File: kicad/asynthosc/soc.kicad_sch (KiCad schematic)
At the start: 46 parts, among them J3 Conn_ARM_SWD_TagConnect_TC203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, J4 Conn_02x07_Odd_Even, J5 Conn_02x04_Odd_Even, SW1 SW_Push, U6 STM32F723VETx, U7 W25Q32JVSS, Y1 8MHz, 8pF

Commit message: sch: pcb: tiny fixes and changes
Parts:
- added C58: 2.2u X7R, Capacitor_SMD:C_0402_1005Metric, symbol Device:C
- added J15: Conn_02x04_Odd_Even, Connector_PinHeader_2.54mm:PinHeader_2x04_P2.54mm_Vertical_SMD, symbol Connector_Generic:Conn_02x04_Odd_Even
- added R83: 3k, Resistor_SMD:R_0402_1005Metric, symbol Device:R
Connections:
- net DBG_LED: now also U6.17 (PC2)
- net GND: now also C58.2, R83.2
- net OTGHS_EXTR: now reaches U6.53 (REXTPHYHS)
- net OTGHS_EXTR: now also R83.1
- net OTGHS_VDD12: now reaches U6.55 (V12PHYHS)
- net OTGHS_VDD12: now also C58.1
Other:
- note added: "External LED GPIO"
- note added: "OTG_HS_REXT"
- note added: "VDD12OTGHS"

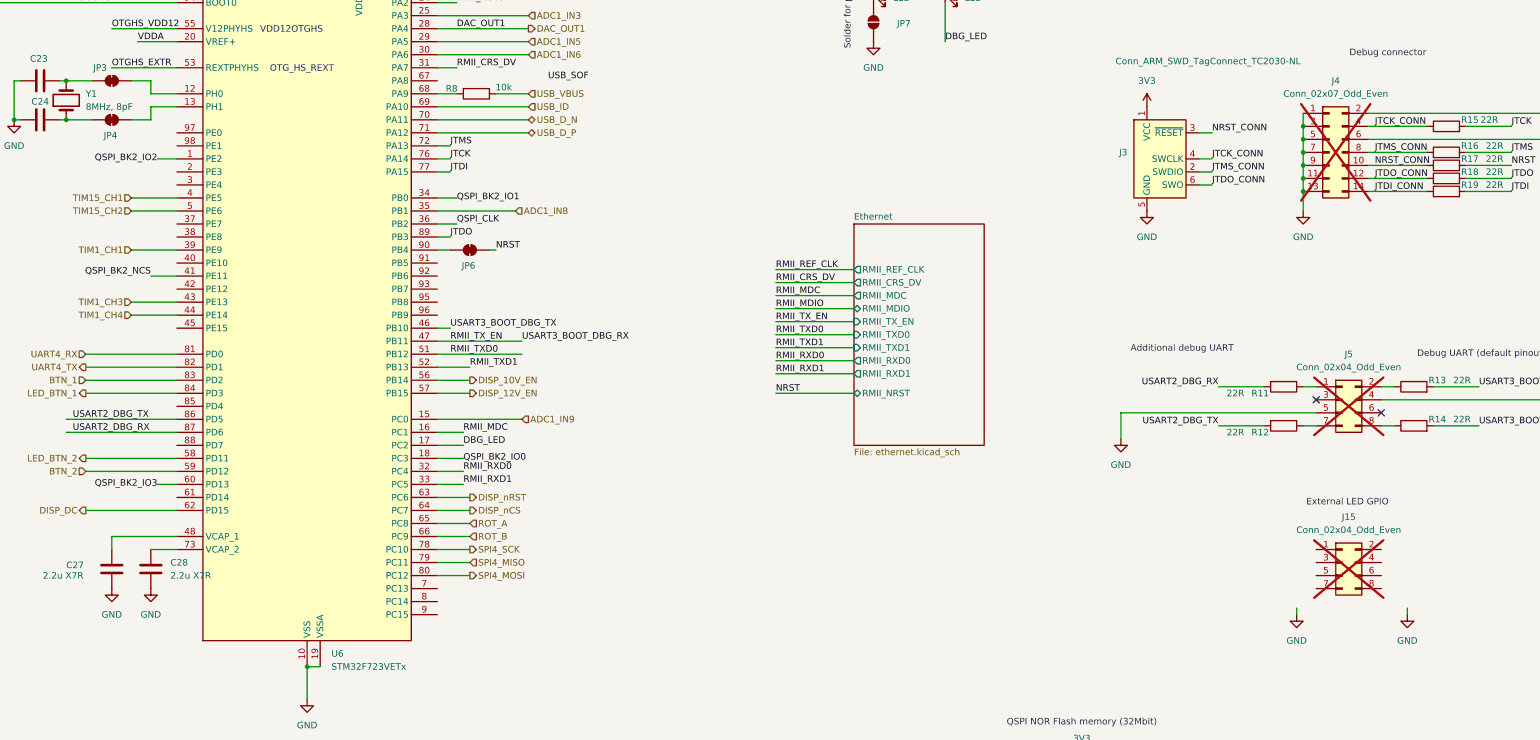
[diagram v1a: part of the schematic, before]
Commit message: sch: pcb: add gpio output connector for optional LEDs on decorative board
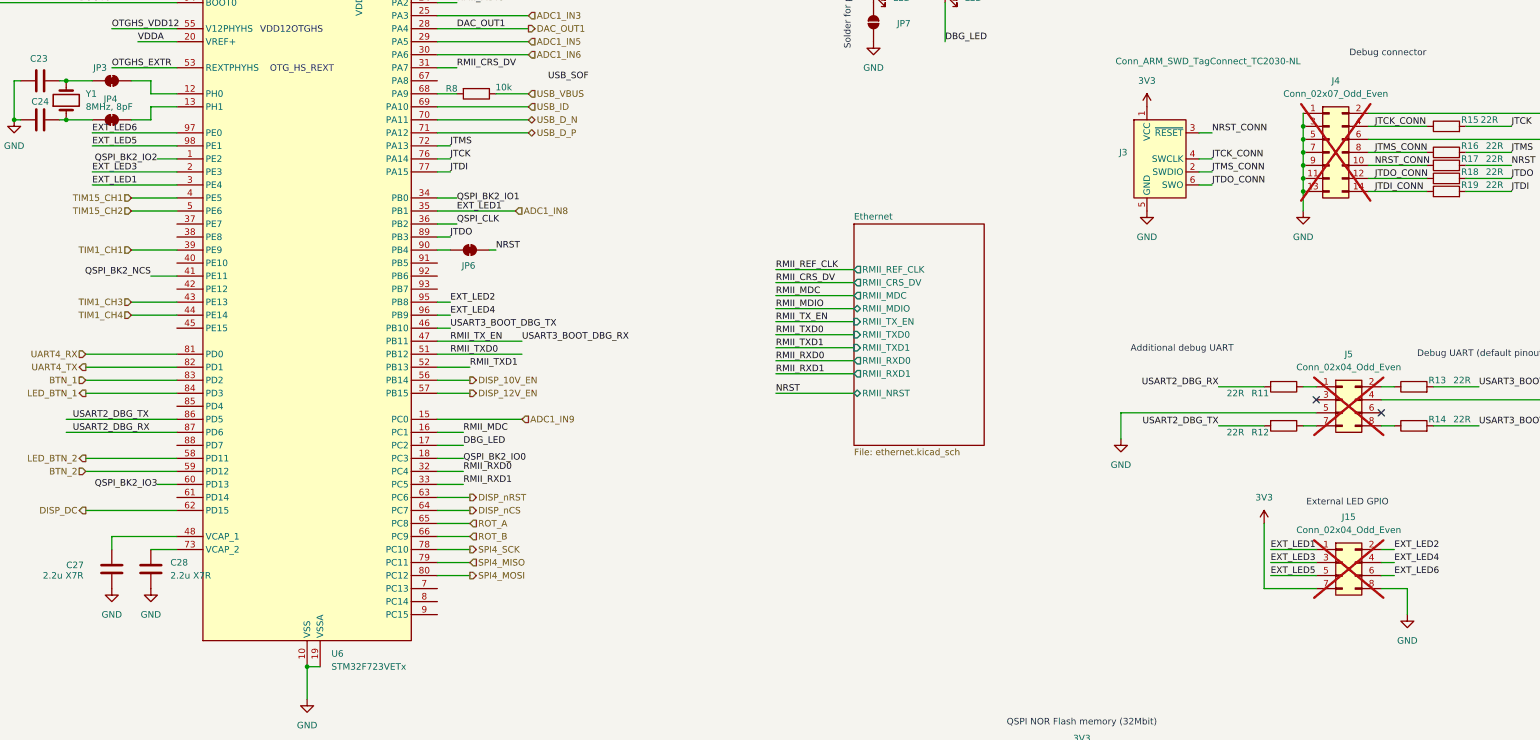
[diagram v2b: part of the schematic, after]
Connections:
- net 3V3: now also J15.7 (Pin_7)
- net ADC1_IN8: now also J15.1 (Pin_1), U6.3 (PE4)
- net GND: now also J15.8 (Pin_8)
- net EXT_LED2: now reaches J15.2 (Pin_2)
- net EXT_LED2: now also U6.95 (PB8)
- net EXT_LED3: now reaches J15.3 (Pin_3)
- net EXT_LED3: now also U6.2 (PE3)
- net EXT_LED4: now reaches J15.4 (Pin_4)
- net EXT_LED4: now also U6.96 (PB9)
- net EXT_LED5: now reaches J15.5 (Pin_5)
- net EXT_LED5: now also U6.98 (PE1)
- net EXT_LED6: now reaches J15.6 (Pin_6)
- net EXT_LED6: now also U6.97 (PE0)

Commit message: sch: pcb: wip and silkscreen cleaning
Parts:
- added JP11: SolderJumper_2_Bridged, asynthosc:SolderJumper_0402_1005Metric_Bridged, symbol Jumper:SolderJumper_2_Bridged
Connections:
- net 3V3: now also JP11.2 (B)
- net at U6.54 (VDDPHYHS): now also JP11.1 (A)
- net ADC1_IN8 renamed EXT_LED1
- net NRST renamed nRST
- net TIM15_CH1: no longer names the net of U6.4 (PE5)
- net TIM15_CH2: no longer names the net of U6.5 (PE6)
- net TIM1_CH1: no longer names the net of U6.39 (PE9)
- no-connect marks 2 -> 20

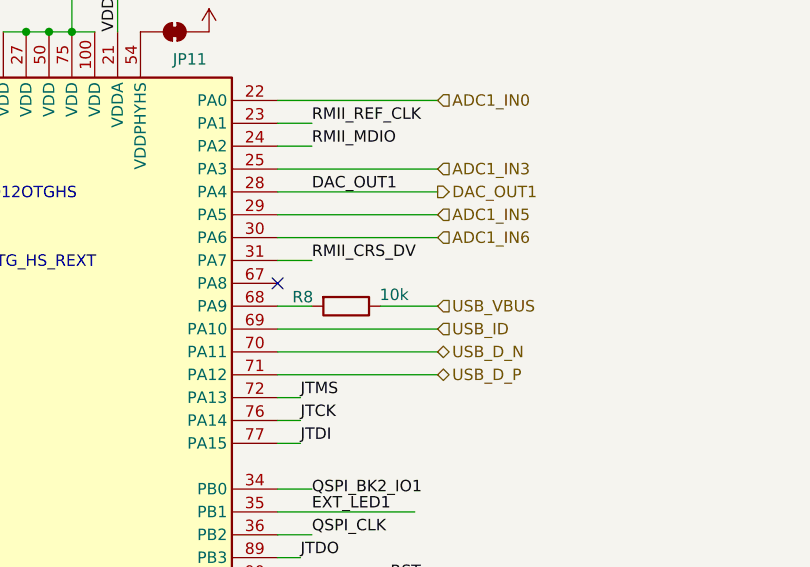
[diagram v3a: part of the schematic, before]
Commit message: sch: pcb: fix: footprint mismatches
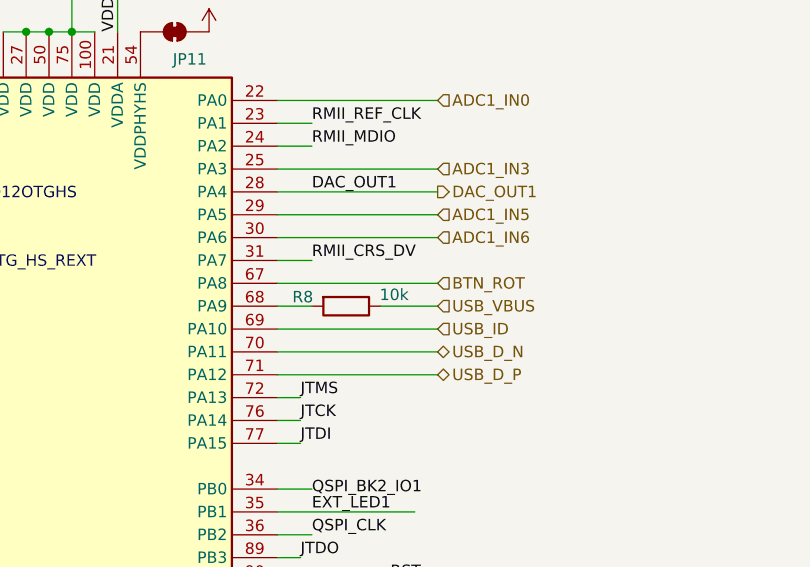
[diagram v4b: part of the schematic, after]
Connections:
- net BTN_ROT: now reaches U6.67 (PA8)
- no-connect marks 20 -> 19
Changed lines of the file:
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@@
-	)
-	(no_connect
-		(at 152.4 72.39)
 	)
 	(no_connect
@@
 		(pts
 			(xy 62.23 20.32) (xy 68.58 20.32)
+		)
+		(stroke
+			(width 0)
+			(type default)
+		)
+	)
+	(wire
+		(pts
+			(xy 152.4 72.39) (xy 170.18 72.39)
 		)
 		(stroke
@@
 		(fields_autoplaced yes)
 		(effects
+			(font
+				(size 1.27 1.27)
+			)
+			(justify left)
+		)
+	)
+	(hierarchical_label "BTN_ROT"
+		(shape input)
+		(at 170.18 72.39 0)
+		(fields_autoplaced yes)
+		(effects

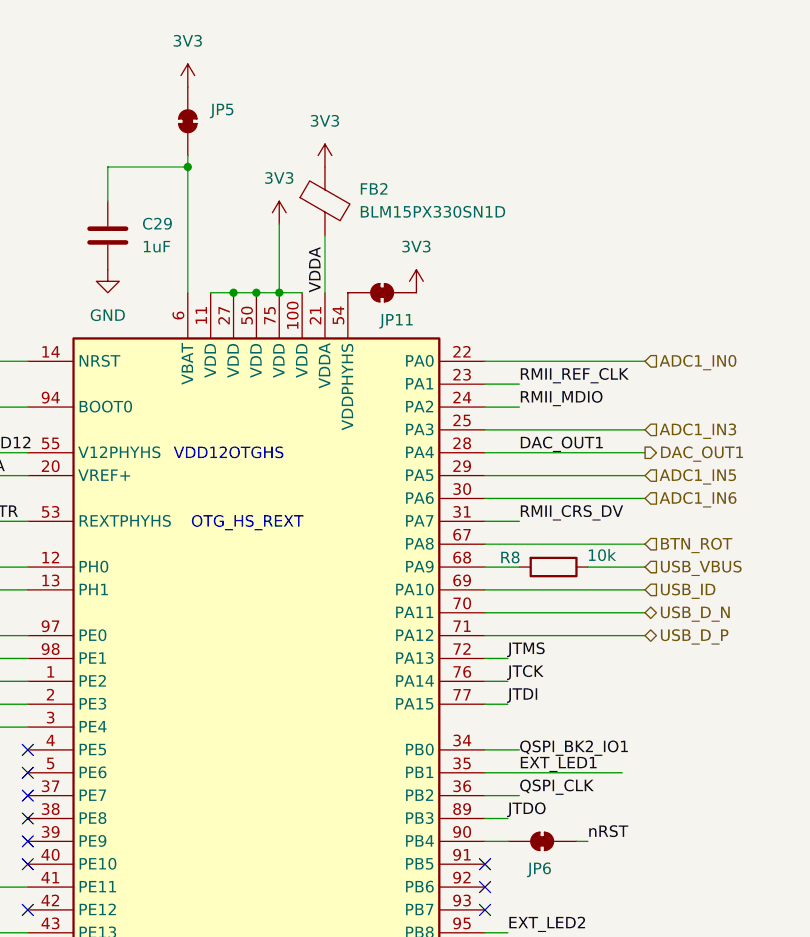
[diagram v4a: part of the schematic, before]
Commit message: pcb: route, add some silkscreen
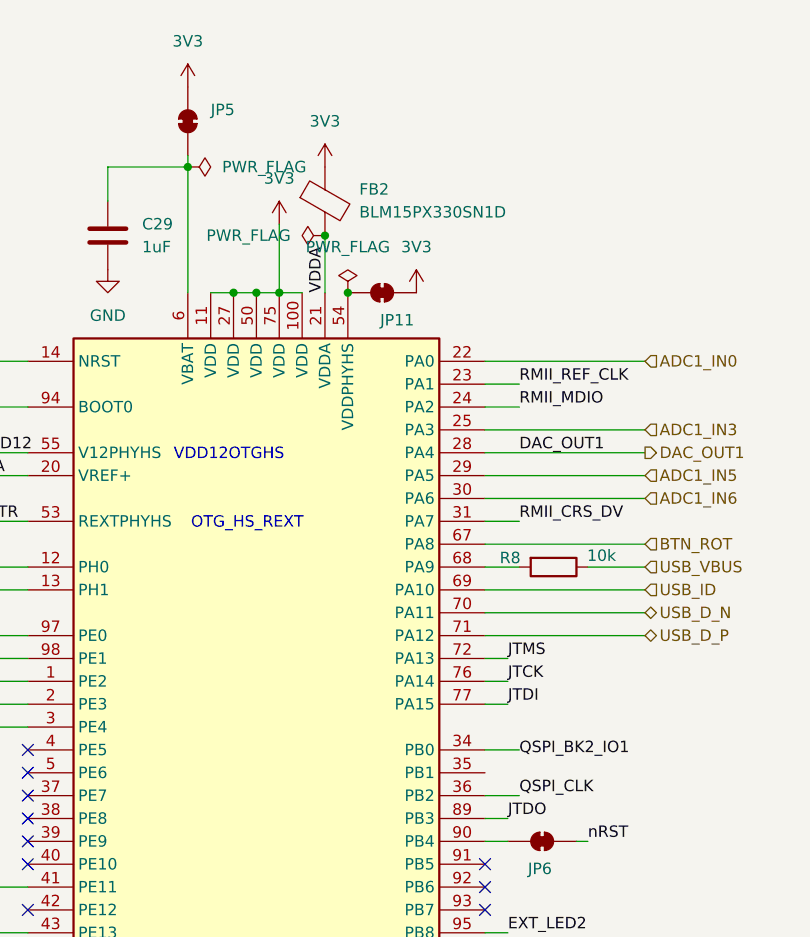
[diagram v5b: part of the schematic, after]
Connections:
- net EXT_LED1: no longer U6.35 (PB1)
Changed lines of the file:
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@@
 	)
 	(junction
+		(at 137.16 44.45)
+		(diameter 0)
+		(color 0 0 0 0)
+	)
+	(junction
 		(at 321.31 81.28)
 		(diameter 0)
@@
 	)
 	(junction
+		(at 134.62 38.1)
+		(diameter 0)
+		(color 0 0 0 0)
+	)
+	(junction
 		(at 321.31 91.44)
 		(diameter 0)
@@
 	(wire
 		(pts
-			(xy 152.4 97.79) (xy 167.64 97.79)
-		)
-		(stroke
-			(width 0)
-			(type default)
-		)
-	)
-	(wire
-		(pts
 			(xy 152.4 87.63) (xy 154.94 87.63)
 		)
@@
 		)
 	)
-	(label "EXT_LED1"
-		(at 156.21 97.79 0)
-		(fields_autoplaced yes)
-		(effects
-			(font
-				(size 1.27 1.27)
-			)
-			(justify left bottom)
-		)
-	)
 	(label "EXT_LED6"
 		(at 339.09 168.91 0)
@@
 	)
 	(symbol
+		(lib_id "power:PWR_FLAG")
+		(at 119.38 30.48 270)
+		(unit 1)
+		(exclude_from_sim no)
+		(in_bom yes)
+		(on_board yes)
+		(dnp no)
+		(fields_autoplaced yes)
+		(property "Reference" "#FLG08"
+			(at 121.285 30.48 0)
+			(effects
+				(font
+					(size 1.27 1.27)
+				)
+				(hide yes)
+			)
+		)
+		(property "Value" "PWR_FLAG"
+			(at 123.19 30.4799 90)
+			(effects
+				(font
+					(size 1.27 1.27)
+				)
+				(justify left)
+			)
+		)
+		(property "Footprint" ""
+			(at 119.38 30.48 0)
+			(effects
+				(font
+					(size 1.27 1.27)
+				)
+				(hide yes)
+			)
+		)
+		(property "Datasheet" "~"
+			(at 119.38 30.48 0)
+			(effects
+				(font
+					(size 1.27 1.27)
+				)
+				(hide yes)
+			)
+		)
+		(property "Description" "Special symbol for telling ERC where power comes from"
+			(at 119.38 30.48 0)
+			(effects
+				(font
+					(size 1.27 1.27)
+				)
+				(hide yes)
+			)
+		)
+		(pin "1"
+		)
+		(instances
+			(project "asynthosc"
+				(path "/d73e377a-a016-415f-8824-91cc6e4907b9/dee5e89d-6774-4f8d-b6d8-6a859b9e32e8"
+					(reference "#FLG08")
+					(unit 1)
+				)
+			)
+		)
+	)
+	(symbol
 		(lib_id "power:GND")
 		(at 285.75 142.24 0)
@@
 	)
 	(symbol
+		(lib_id "power:PWR_FLAG")
+		(at 134.62 38.1 90)
+		(unit 1)
+		(exclude_from_sim no)
+		(in_bom yes)
+		(on_board yes)
+		(dnp no)
+		(fields_autoplaced yes)
+		(property "Reference" "#FLG02"
+			(at 132.715 38.1 0)
+			(effects
+				(font
+					(size 1.27 1.27)
+				)
+				(hide yes)
+			)
+		)
+		(property "Value" "PWR_FLAG"
+			(at 130.81 38.0999 90)
+			(effects
+				(font
+					(size 1.27 1.27)
+				)
+				(justify left)
+			)
+		)
+		(property "Footprint" ""
+			(at 134.62 38.1 0)
+			(effects
+				(font
+					(size 1.27 1.27)
+				)
+				(hide yes)
+			)
+		)
+		(property "Datasheet" "~"
+			(at 134.62 38.1 0)
+			(effects
+				(font
+					(size 1.27 1.27)
+				)
+				(hide yes)
+			)
+		)
+		(property "Description" "Special symbol for telling ERC where power comes from"
+			(at 134.62 38.1 0)
+			(effects
+				(font
+					(size 1.27 1.27)
+				)
+				(hide yes)
+			)
+		)
+		(pin "1"
+		)
+		(instances
+			(project ""
+				(path "/d73e377a-a016-415f-8824-91cc6e4907b9/dee5e89d-6774-4f8d-b6d8-6a859b9e32e8"
+					(reference "#FLG02")
+					(unit 1)
+				)
+			)
+		)
+	)
+	(symbol
 		(lib_id "power:+3V3")
 		(at 24.13 20.32 0)
@@
 					(unit 1)
 				)
+			)
+		)
+	)
+	(symbol
+		(lib_id "power:PWR_FLAG")
+		(at 137.16 44.45 0)
+		(unit 1)
+		(exclude_from_sim no)
+		(in_bom yes)
+		(on_board yes)
+		(dnp no)
+		(fields_autoplaced yes)
+		(property "Reference" "#FLG07"
+			(at 137.16 42.545 0)
+			(effects
+				(font
+					(size 1.27 1.27)
+				)
+				(hide yes)
+			)
+		)
+		(property "Value" "PWR_FLAG"
+			(at 137.16 39.37 0)
+			(effects
+				(font
+					(size 1.27 1.27)
+				)
+			)
+		)
+		(property "Footprint" ""
+			(at 137.16 44.45 0)
+			(effects
+				(font
+					(size 1.27 1.27)
+				)
+				(hide yes)
+			)
+		)
+		(property "Datasheet" "~"
+			(at 137.16 44.45 0)
+			(effects
+				(font
+					(size 1.27 1.27)
+				)
+				(hide yes)
+			)
+		)
+		(property "Description" "Special symbol for telling ERC where power comes from"
+			(at 137.16 44.45 0)
+			(effects
+				(font
+					(size 1.27 1.27)
+				)
+				(hide yes)
+			)
+		)
+		(pin "1"
+		)
+		(instances
+			(project "asynthosc"
+				(path "/d73e377a-a016-415f-8824-91cc6e4907b9/dee5e89d-6774-4f8d-b6d8-6a859b9e32e8"
+					(reference "#FLG07")
+					(unit 1)
+				)
